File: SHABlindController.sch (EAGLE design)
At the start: 37 parts, among them IC1 SPARKCORE, IC2 RAC02-05SC, IC5 RXB1SIL, Q1 2N7002, Q2 2N7002

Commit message: Release v3.0
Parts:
- removed C4: 1uF 0603, freetronics:CAP0603
- removed JP11: ACTIVE2, freetronics-master-v1.1:M01PTH_LARGE
- added C1: 1uF 0603, freetronics:CAP0603
- added JP3: ACTIVE1, freetronics-master-v1.1:M01PTH_LARGE
- C2: value 1uF 0603 -> 10uF 6.3V A TANT; device freetronics:CAP0603 -> freetronics:CAP_POL1206
- C3: value 10uF 6.3V A TANT -> 1uF 0603; device freetronics:CAP_POL1206 -> freetronics:CAP0603
- JP10: value ACTIVE2 -> EARTH
- JP4: value EARTH -> ACTIVE1
- JP5, JP9: value ACTIVE1 -> ACTIVE2
- renumbered IC5 to IC3
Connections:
- net EARTH: now also JP10.1; no longer JP4.1
- net GND: now also C1.2, C2.-, C3.2; no longer C2.2, C3.-, C4.2
- net N$14: now also JP4.1; no longer JP5.1
- net N$7: now also JP3.1; no longer JP9.1
- net N$8: now also JP5.1, JP9.1; no longer JP10.1, JP11.1
- net VCC: now also C3.1; no longer C4.1
- net VIN: now also C1.1, C2.+; no longer C2.1, C3.+
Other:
- moved on the sheet: JP10, JP4, JP5, JP8, JP9

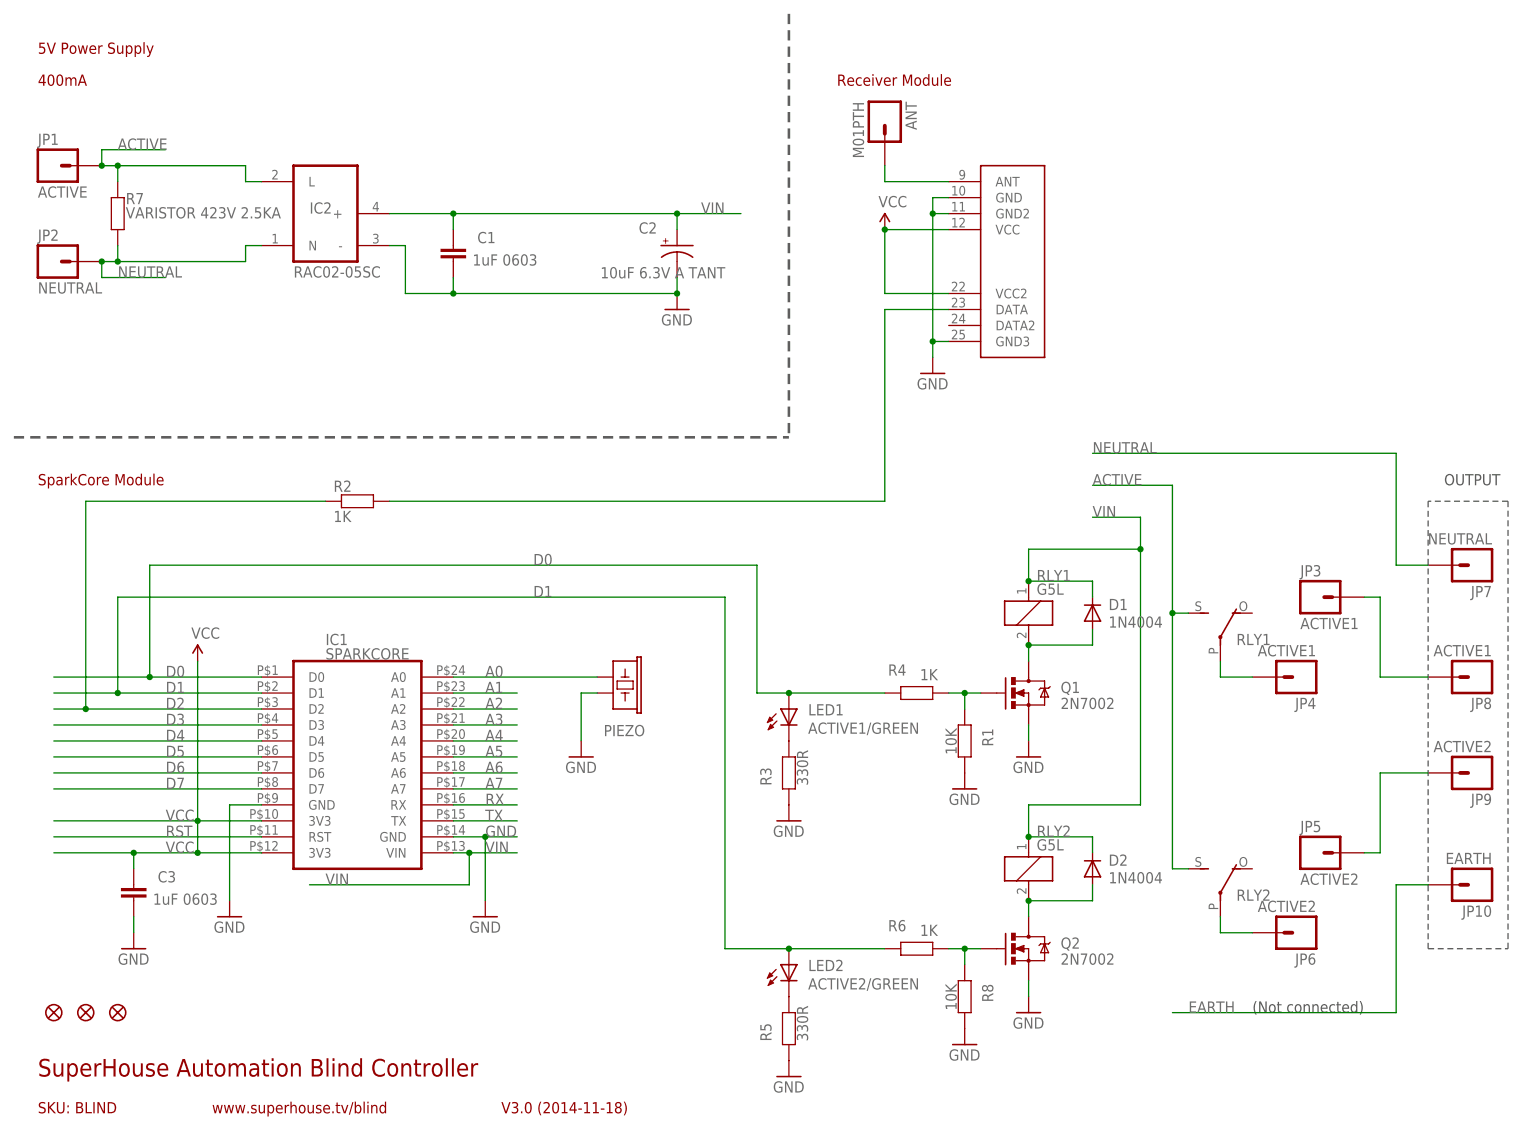
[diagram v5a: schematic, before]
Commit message: v4.0 release: improved 433MHz rx footprint, added PTH option for piezo
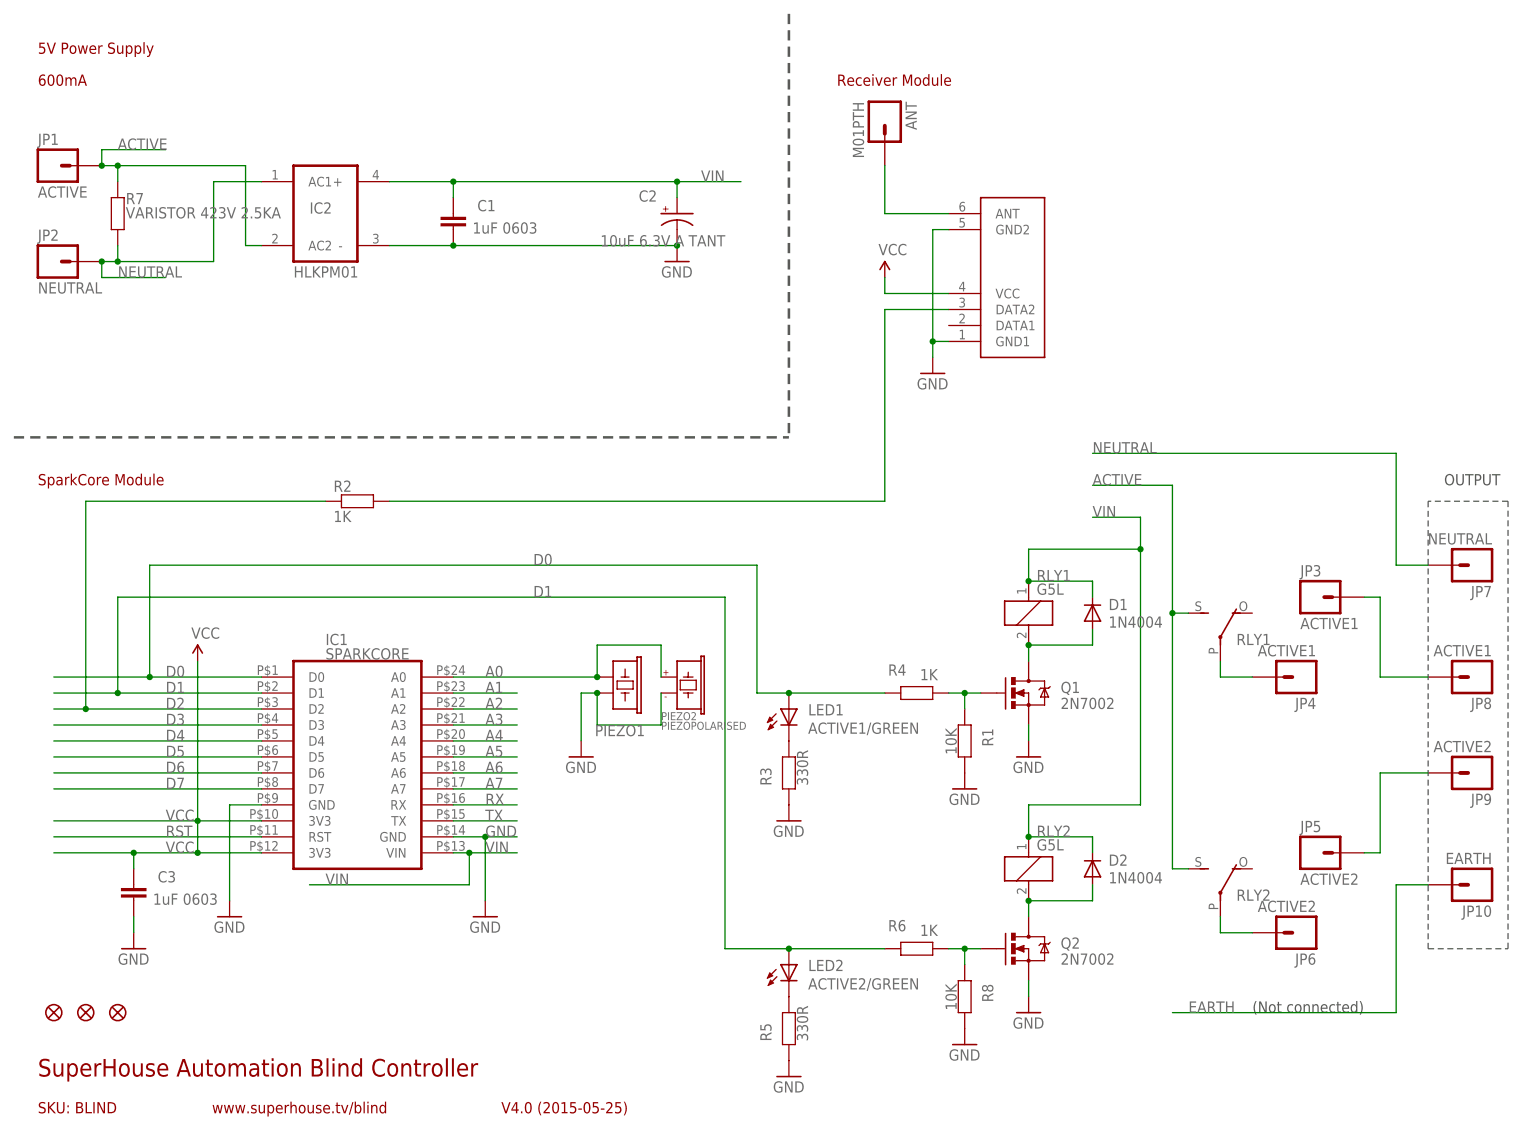
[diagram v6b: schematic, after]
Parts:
- added PIEZO2: PIEZOPOLARISED, freetronics-jon:PIEZOPOLARISED
- IC2: value RAC02-05SC -> HLKPM01; device freetronics-jon:RAC0X-SC -> freetronics-jon:HLKPM01
- IC3: value RXB1SIL -> RXB1; device PracticalArduino:RXB1SIL -> freetronics-master-v1:RXB1SHORTFLAT
- renumbered PIEZO to PIEZO1
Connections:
- net A0: now also PIEZO2.+
- net ACTIVE: now also IC2.AC2; no longer IC2.L
- net GND: now also IC3.GND1, PIEZO2.-; no longer IC3.GND, IC3.GND3
- net N$135: now also IC3.DATA2; no longer IC3.DATA
- net NEUTRAL: now also IC2.AC1; no longer IC2.N
- net VCC: no longer IC3.VCC2
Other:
- note added: "600mA"
- note added: "V4.0 (2015-05-25)"
- note removed: "400mA"
- note removed: "V3.0 (2014-11-18)"
- moved on the sheet: C1, C2

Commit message: v4.1 release: Added fuse mount; added Molex 15-24-4441 (8981 series) connector
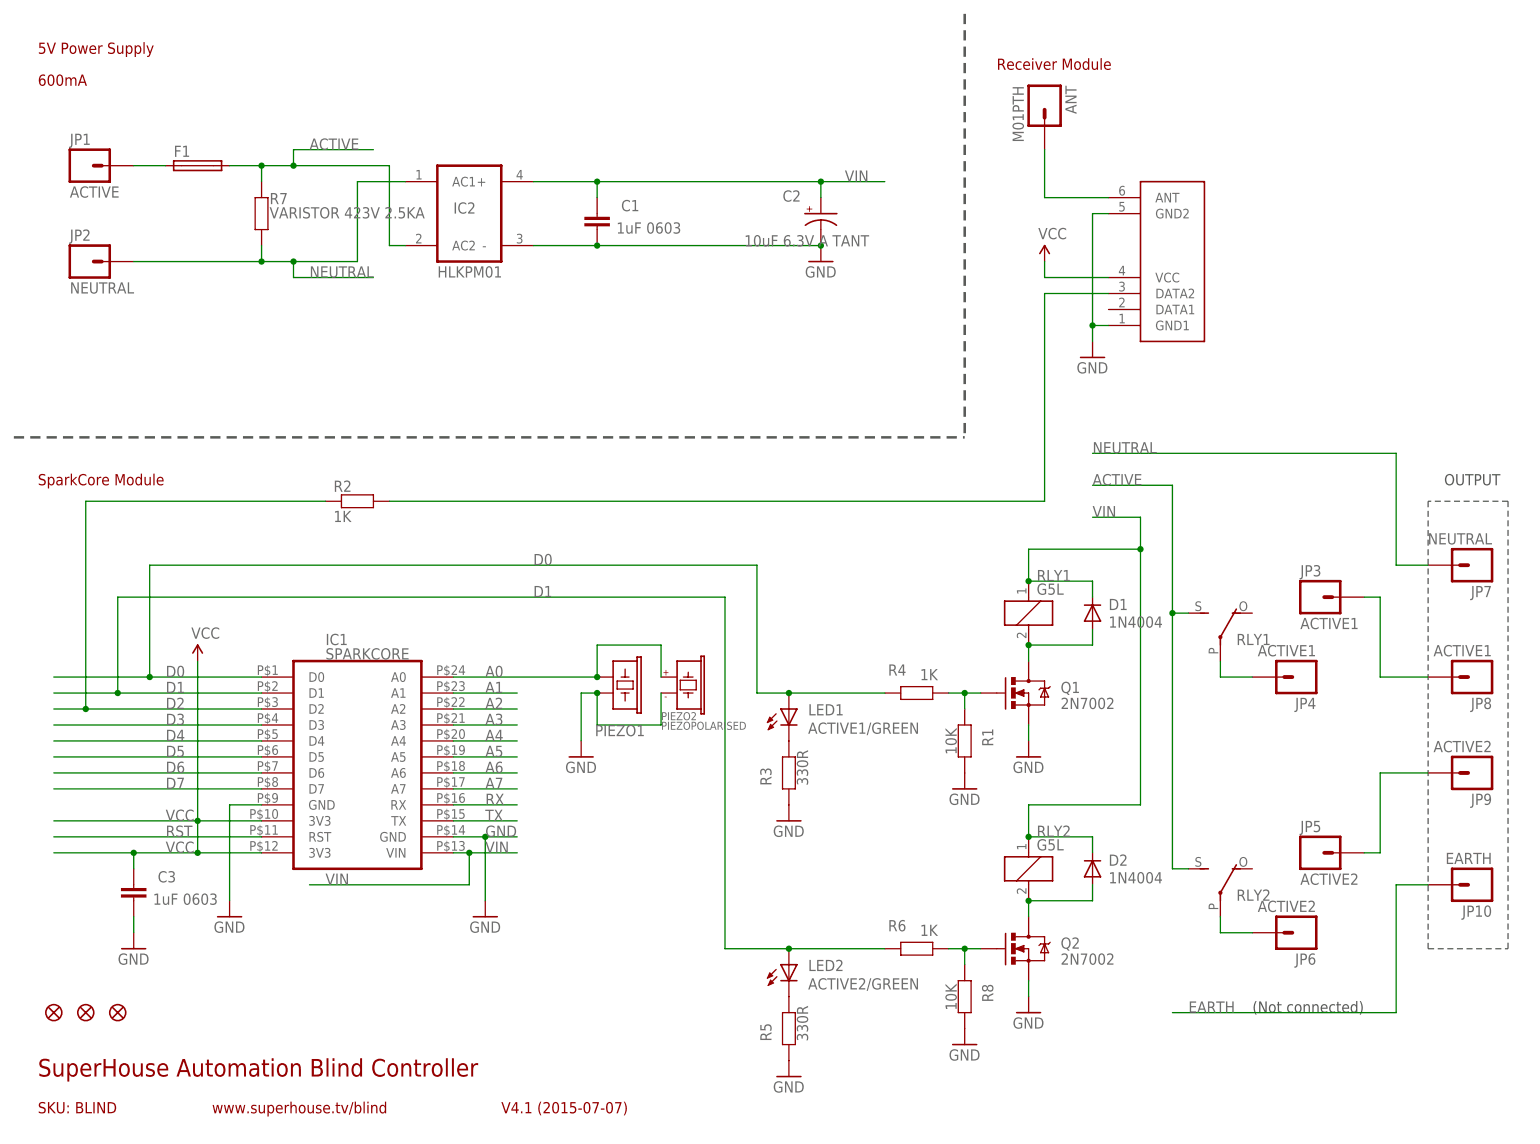
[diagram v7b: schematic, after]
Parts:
- added F1: (no value), freetronics-jon:PICOFUSE
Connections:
- new net N$9: F1.1, JP1.1
- net ACTIVE: now also F1.2; no longer JP1.1
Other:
- note added: "V4.1 (2015-07-07)"
- note removed: "V4.0 (2015-05-25)"
- moved on the sheet: ANT, C1, C2, IC2, JP1, JP2, R7

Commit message: Added value to fuse
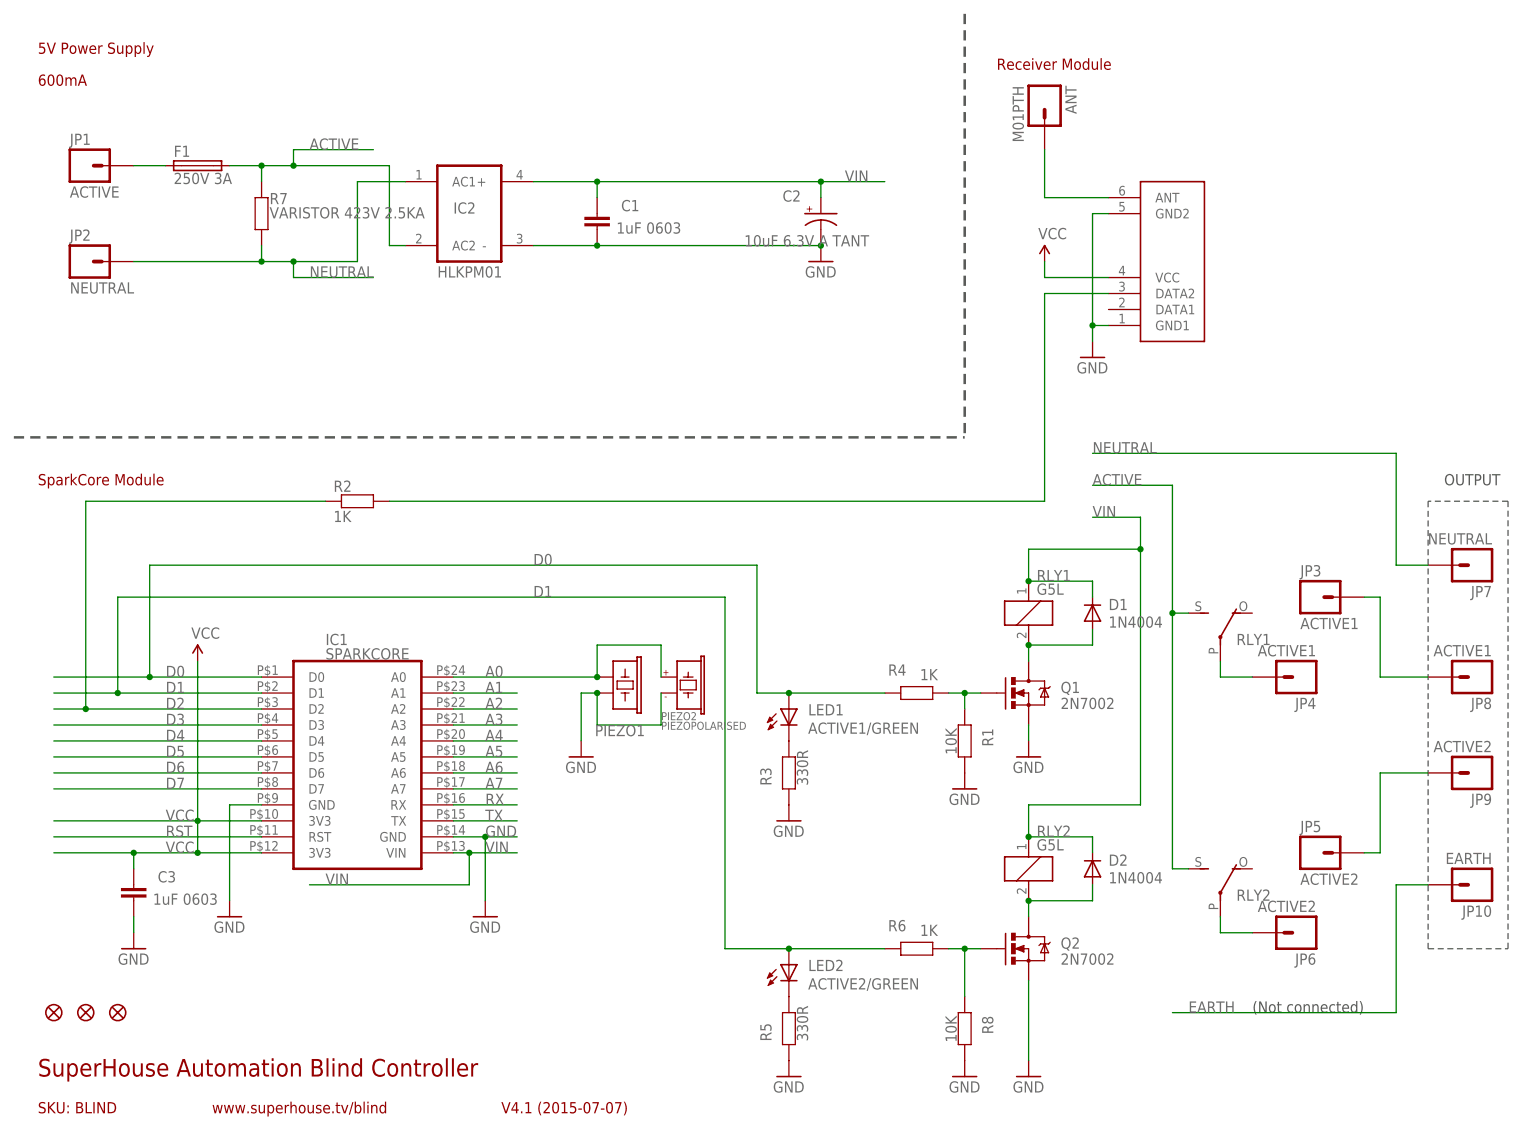
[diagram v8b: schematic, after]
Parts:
- F1: value (none) -> 250V 3A
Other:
- moved on the sheet: R8
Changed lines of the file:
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@@
 <part name="PIEZO2" library="freetronics-jon" deviceset="PIEZOPOLARISED" device=""/>
 <part name="IC2" library="freetronics-jon" deviceset="HLKPM01" device=""/>
-<part name="F1" library="freetronics-jon" deviceset="PICOFUSE" device=""/>
+<part name="F1" library="freetronics-jon" deviceset="PICOFUSE" device="" value="250V 3A"/>
 </parts>
 <sheets>
@@
 <attribute name="VALUE" x="147.828" y="35.052" size="1.778" layer="96"/>
 </instance>
-<instance part="GND8" gate="1" x="165.1" y="22.86"/>
+<instance part="GND8" gate="1" x="165.1" y="12.7"/>
 <instance part="GND9" gate="1" x="165.1" y="63.5"/>
 <instance part="D1" gate="G$1" x="175.26" y="86.36" smashed="yes" rot="R90">
@@
 </instance>
 <instance part="GND11" gate="1" x="154.94" y="58.42"/>
-<instance part="R8" gate="G$1" x="154.94" y="25.4" smashed="yes" rot="R270">
-<attribute name="NAME" x="157.7086" y="27.432" size="1.778" layer="95" rot="R270"/>
-<attribute name="VALUE" x="151.892" y="27.432" size="1.778" layer="96" rot="R270"/>
-</instance>
-<instance part="GND12" gate="1" x="154.94" y="17.78"/>
+<instance part="R8" gate="G$1" x="154.94" y="20.32" smashed="yes" rot="R270">
+<attribute name="NAME" x="157.7086" y="22.352" size="1.778" layer="95" rot="R270"/>
+<attribute name="VALUE" x="151.892" y="22.352" size="1.778" layer="96" rot="R270"/>
+</instance>
+<instance part="GND12" gate="1" x="154.94" y="12.7"/>
 <instance part="IC3" gate="G$1" x="187.96" y="144.78" rot="MR90"/>
 <instance part="PIEZO2" gate="G$1" x="109.22" y="73.66"/>
@@
 <pinref part="Q2" gate="G$1" pin="S"/>
 <pinref part="GND8" gate="1" pin="GND"/>
-<wire x1="165.1" y1="25.4" x2="165.1" y2="27.94" width="0.1524" layer="91"/>
+<wire x1="165.1" y1="15.24" x2="165.1" y2="27.94" width="0.1524" layer="91"/>
 </segment>
 <segment>
@@
 <pinref part="R8" gate="G$1" pin="1"/>
 <wire x1="154.94" y1="33.02" x2="157.48" y2="33.02" width="0.1524" layer="91"/>
-<wire x1="154.94" y1="30.48" x2="154.94" y2="33.02" width="0.1524" layer="91"/>
+<wire x1="154.94" y1="25.4" x2="154.94" y2="33.02" width="0.1524" layer="91"/>
 <junction x="154.94" y="33.02"/>
 </segment>
